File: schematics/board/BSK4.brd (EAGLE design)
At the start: 82 x 100 mm, 22 parts

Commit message: Реструктурированы сигналы коммутации для плат БСК
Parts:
- renumbered VAR3 to BSK1, VAR4 to PAYLOAD
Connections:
- net KEM10 renamed B4_KEM-
- net KEM9 renamed B4_KEM+
- net KHEAT5 renamed B4_KHEAT
- net KVCC5 renamed B4_KVCC
- net VCCL renamed PL_KVCC
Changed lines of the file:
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@@
 <attribute name="NAME" x="25.265" y="83.035" size="1.27" layer="25"/>
 </element>
-<element name="VAR3" library="pinheadCS" package="1X14" value="" x="41" y="98.75" smashed="yes">
+<element name="BSK1" library="pinheadCS" package="1X14" value="" x="41" y="98.75" smashed="yes">
 <attribute name="NAME" x="24.1438" y="95.5788" size="1.27" layer="25" ratio="10"/>
 <attribute name="VALUE" x="23.22" y="95.575" size="1.27" layer="27"/>
 </element>
-<element name="VAR4" library="pinheadCS" package="1X08" value="" x="41" y="24" smashed="yes">
+<element name="PAYLOAD" library="pinheadCS" package="1X08" value="" x="41" y="24" smashed="yes">
 <attribute name="NAME" x="30.7638" y="25.8288" size="1.27" layer="25" ratio="10"/>
 <attribute name="VALUE" x="30.84" y="20.825" size="1.27" layer="27"/>
@@
 <contactref element="U$8" pad="17"/>
 <contactref element="U$9" pad="67"/>
-<contactref element="VAR3" pad="9"/>
+<contactref element="BSK1" pad="9"/>
 <contactref element="U$10" pad="67"/>
 <wire x1="33.5" y1="88" x2="33.36" y2="87.74" width="0.3" layer="1"/>
@@
 <contactref element="U$8" pad="20"/>
 <contactref element="U$5" pad="3"/>
-<contactref element="VAR3" pad="2"/>
-<contactref element="VAR4" pad="3"/>
+<contactref element="BSK1" pad="2"/>
+<contactref element="PAYLOAD" pad="3"/>
 <wire x1="46" y1="79.5" x2="45.865" y2="79.32" width="0.3" layer="1"/>
 <wire x1="46" y1="89" x2="45.865" y2="88.92" width="0.3" layer="1"/>
@@
 <signal name="1W">
 <contactref element="U$5" pad="4"/>
-<contactref element="VAR3" pad="14"/>
+<contactref element="BSK1" pad="14"/>
 <wire x1="36" y1="71" x2="36" y2="72" width="0.3" layer="1"/>
 <wire x1="42" y1="71" x2="36" y2="71" width="0.3" layer="16"/>
@@
 <via x="59" y="76.5" extent="1-16" drill="0.35"/>
 </signal>
-<signal name="KEM9">
+<signal name="B4_KEM+">
 <contactref element="U$8" pad="2"/>
-<contactref element="VAR3" pad="11"/>
+<contactref element="BSK1" pad="11"/>
 <wire x1="56" y1="90.5" x2="56" y2="89" width="0.3" layer="1"/>
 <wire x1="56" y1="92.5" x2="56" y2="90.5" width="0.3" layer="16"/>
@@
 <via x="56" y="90.5" extent="1-16" drill="0.35"/>
 </signal>
-<signal name="KEM10">
+<signal name="B4_KEM-">
 <contactref element="U$8" pad="9"/>
-<contactref element="VAR3" pad="10"/>
+<contactref element="BSK1" pad="10"/>
 <wire x1="47" y1="89.5" x2="47" y2="89" width="0.3" layer="1"/>
 <wire x1="50" y1="92.5" x2="47" y2="89.5" width="0.3" layer="1"/>
@@
 <via x="50" y="92.5" extent="1-16" drill="0.35"/>
 </signal>
-<signal name="KHEAT5">
+<signal name="B4_KHEAT">
 <contactref element="U$8" pad="19"/>
-<contactref element="VAR3" pad="12"/>
+<contactref element="BSK1" pad="12"/>
 <wire x1="56" y1="77.5" x2="56" y2="79" width="0.3" layer="1"/>
 <wire x1="56" y1="89.5" x2="56" y2="77.5" width="0.3" layer="16"/>
@@
 </signal>
 <signal name="VDD">
-<contactref element="VAR3" pad="1"/>
-<contactref element="VAR4" pad="2"/>
+<contactref element="BSK1" pad="1"/>
+<contactref element="PAYLOAD" pad="2"/>
 <wire x1="33" y1="22.5" x2="34.5" y2="24" width="0.3" layer="16"/>
 <wire x1="31.5" y1="22.5" x2="33" y2="22.5" width="0.3" layer="16"/>
@@
 <wire x1="24" y1="98.5" x2="24.49" y2="98.75" width="0.3" layer="16"/>
 </signal>
-<signal name="KVCC5">
+<signal name="B4_KVCC">
 <contactref element="R10" pad="1"/>
 <contactref element="R11" pad="1"/>
 <contactref element="R19" pad="1"/>
 <contactref element="R20" pad="1"/>
-<contactref element="VAR3" pad="13"/>
+<contactref element="BSK1" pad="13"/>
 <wire x1="37.5" y1="86" x2="37.7" y2="85.8" width="0.3" layer="1"/>
 <wire x1="36.5" y1="87" x2="37.5" y2="86" width="0.3" layer="1"/>
@@
 </signal>
 <signal name="SDATM">
-<contactref element="VAR3" pad="6"/>
-<contactref element="VAR4" pad="7"/>
+<contactref element="BSK1" pad="6"/>
+<contactref element="PAYLOAD" pad="7"/>
 <wire x1="47.5" y1="31.5" x2="47.5" y2="24" width="0.3" layer="16"/>
 <wire x1="63.5" y1="47.5" x2="47.5" y2="31.5" width="0.3" layer="16"/>
@@
 </signal>
 <signal name="SCLTM">
-<contactref element="VAR3" pad="7"/>
-<contactref element="VAR4" pad="8"/>
+<contactref element="BSK1" pad="7"/>
+<contactref element="PAYLOAD" pad="8"/>
 <wire x1="50" y1="33" x2="50" y2="24" width="0.3" layer="16"/>
 <wire x1="64" y1="47" x2="50" y2="33" width="0.3" layer="16"/>
@@
 <contactref element="U$3" pad="P$1"/>
 <contactref element="U$3" pad="P$2"/>
-<contactref element="VAR3" pad="3"/>
-<contactref element="VAR4" pad="4"/>
+<contactref element="BSK1" pad="3"/>
+<contactref element="PAYLOAD" pad="4"/>
 <wire x1="65.5" y1="74.5" x2="61.5" y2="74.5" width="0.3" layer="1"/>
 <wire x1="61.5" y1="74.5" x2="61.153803125" y2="74.39644375" width="0.3" layer="1"/>
@@
 </signal>
 <signal name="PL-">
-<contactref element="VAR4" pad="1"/>
+<contactref element="PAYLOAD" pad="1"/>
 <contactref element="U$10" pad="23"/>
 <wire x1="29.5" y1="88" x2="29.44" y2="87.76" width="0.3" layer="1"/>
@@
 <wire x1="27.5" y1="82" x2="27.15" y2="81.9" width="0.3" layer="1"/>
 </signal>
-<signal name="VCCL">
+<signal name="PL_KVCC">
 <contactref element="R2" pad="1"/>
 <contactref element="R7" pad="1"/>
-<contactref element="VAR3" pad="8"/>
+<contactref element="BSK1" pad="8"/>
 <wire x1="25.5" y1="82" x2="25.45" y2="81.9" width="0.3" layer="1"/>
 <wire x1="25.5" y1="87" x2="25.45" y2="87.3" width="0.3" layer="1"/>
@@
 </signal>
 <signal name="I2CINT">
-<contactref element="VAR3" pad="5"/>
-<contactref element="VAR4" pad="6"/>
+<contactref element="BSK1" pad="5"/>
+<contactref element="PAYLOAD" pad="6"/>
 <wire x1="40" y1="19.5" x2="44.5" y2="24" width="0.3" layer="16"/>
 <wire x1="15.5" y1="19.5" x2="40" y2="19.5" width="0.3" layer="16"/>
@@
 </signal>
 <signal name="TIME">
-<contactref element="VAR3" pad="4"/>
-<contactref element="VAR4" pad="5"/>
+<contactref element="BSK1" pad="4"/>
+<contactref element="PAYLOAD" pad="5"/>
 <wire x1="44" y1="25.5" x2="42.5" y2="24" width="0.3" layer="16"/>
 <wire x1="45" y1="25.5" x2="44" y2="25.5" width="0.3" layer="16"/>

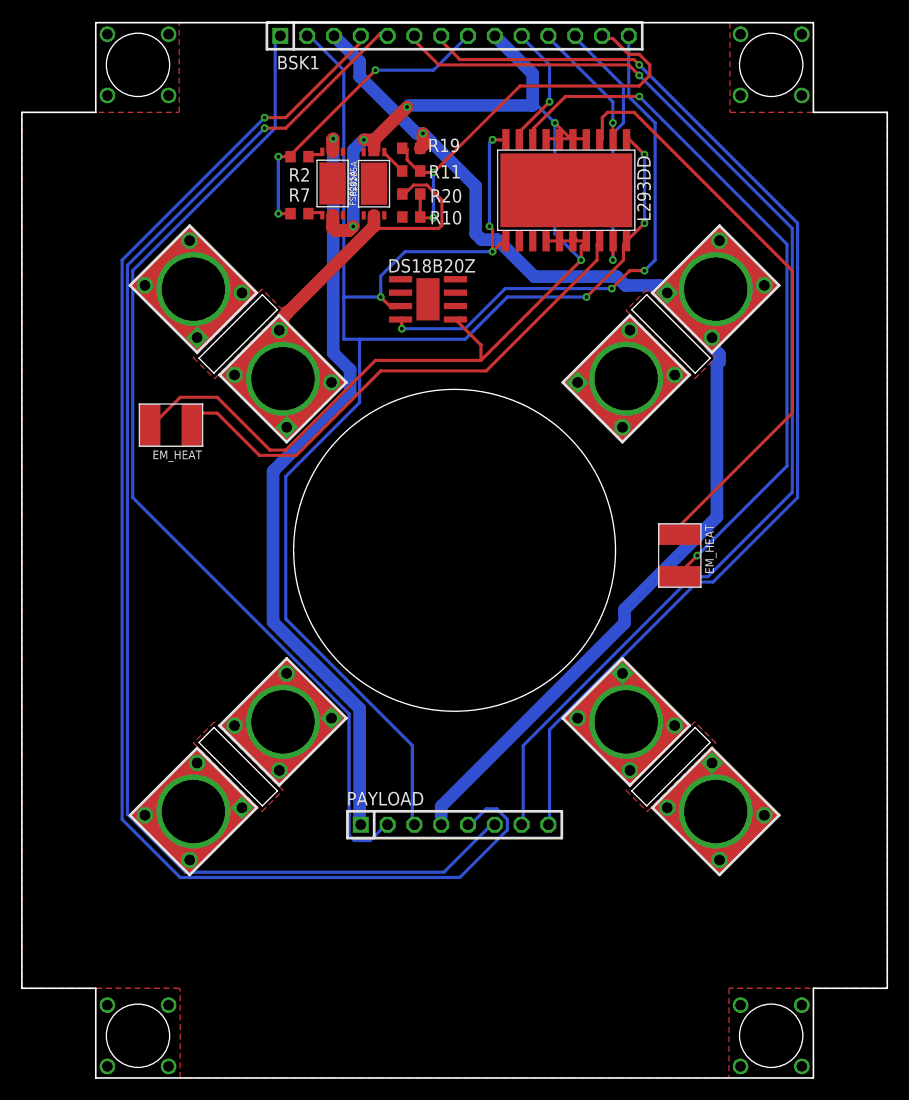
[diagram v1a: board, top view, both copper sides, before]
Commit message: Добавлены светодиоды на платы БСК
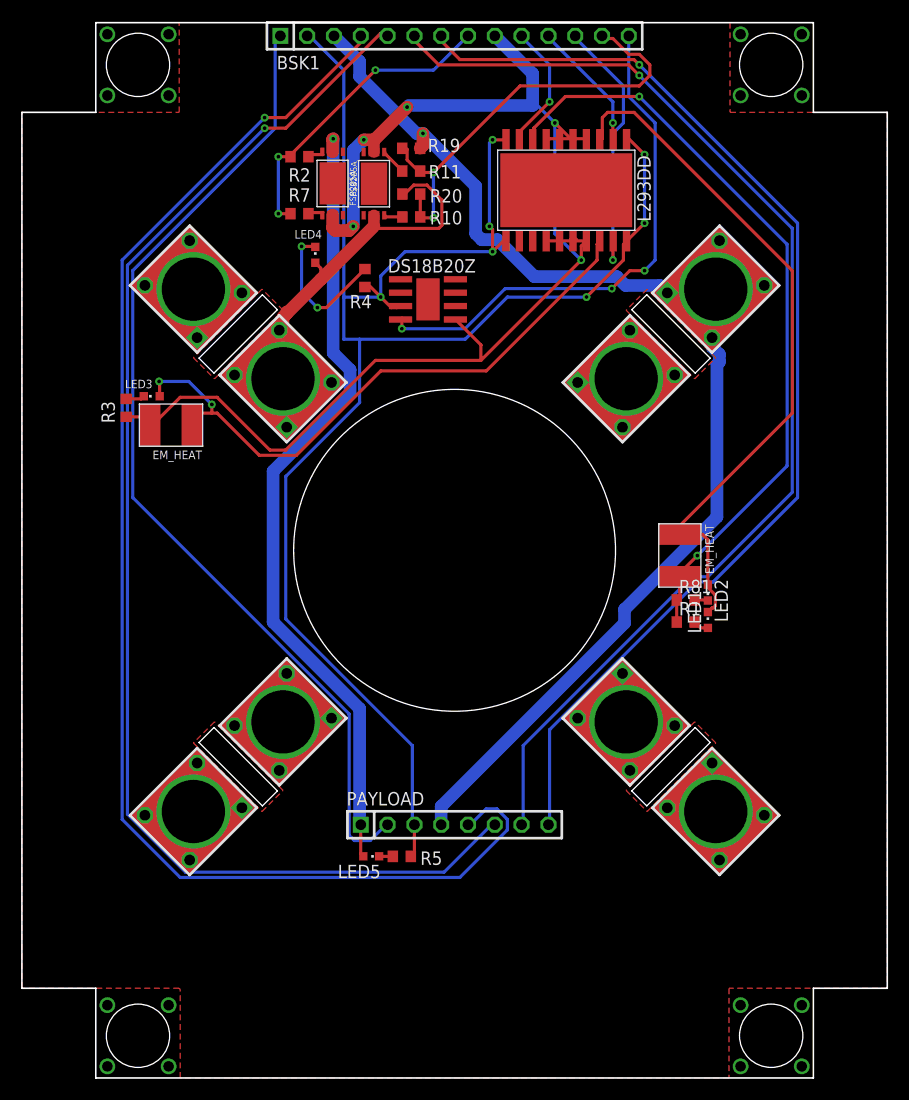
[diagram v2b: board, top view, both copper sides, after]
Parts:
- added LED1, LED2, LED3, LED4, LED5: (no value), led:CHIPLED_0603
- added R1, R3, R4, R5, R81: 2k, resistor:R0603
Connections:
- new net N$10: LED3.C, R3.1
- new net N$27: LED4.C, R4.2
- new net N$28: LED5.C, R5.2
- new net N$5: LED2.C, R81.2
- new net N$7: LED1.A, R1.2
- net 5V: now also R4.1, R5.1
- net BUS-: now also LED4.A
- net GND: now also R3.2
- net N$1: now also LED1.C, LED2.A
- net N$2: now also R1.1, R81.1
- net N$3: now also LED3.A
- net PL-: now also LED5.A
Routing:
- net N$27: track 0.00 -> 13.8 mm, vias 0 -> 2
- net N$1: track 56.3 -> 66.7 mm
- net N$3: track 49.7 -> 59.1 mm, vias 0 -> 2
- net 5V: track 160.7 -> 165.7 mm
- net N$2: track 67.8 -> 72.3 mm
- net PL-: track 73.7 -> 76.8 mm
- net GND: track 125.3 -> 127.9 mm
- net N$8: track 0.00 -> 1.78 mm
- net N$10: track 0.00 -> 1.75 mm
- net BUS-: track 52.0 -> 53.5 mm
- net N$7: track 0.00 -> 1.48 mm
- net N$28: track 0.00 -> 1.30 mm
- net N$5: track 0.00 -> 1.27 mm

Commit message: Разведены платы БСК2-5
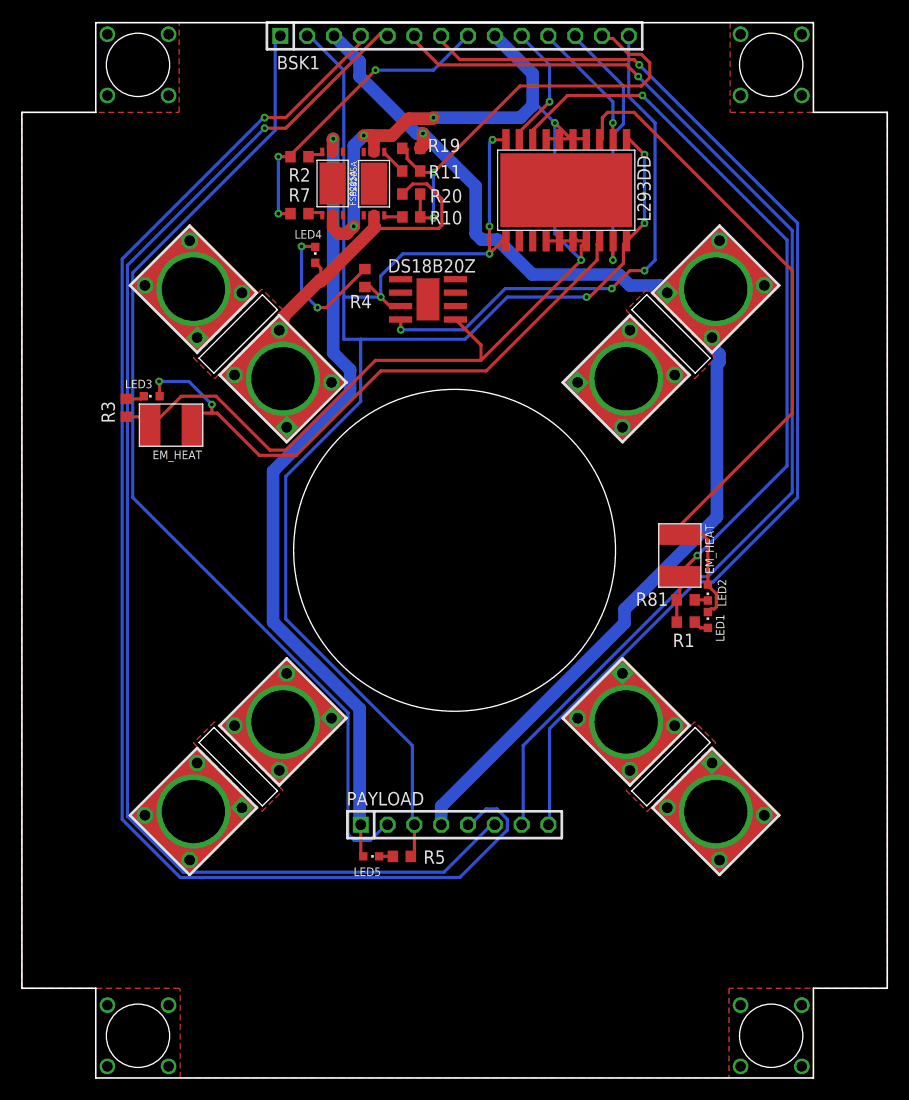
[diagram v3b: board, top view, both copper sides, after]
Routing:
- net GND: track 127.9 -> 128.6 mm
